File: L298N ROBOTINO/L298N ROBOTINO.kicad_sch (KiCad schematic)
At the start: 22 parts, among them J1 Conn_01x03, J2 Conn_01x03, J3 Conn_01x03, J4 Conn_01x02, J5 Conn_01x02, U1 L7805, U2 L298N

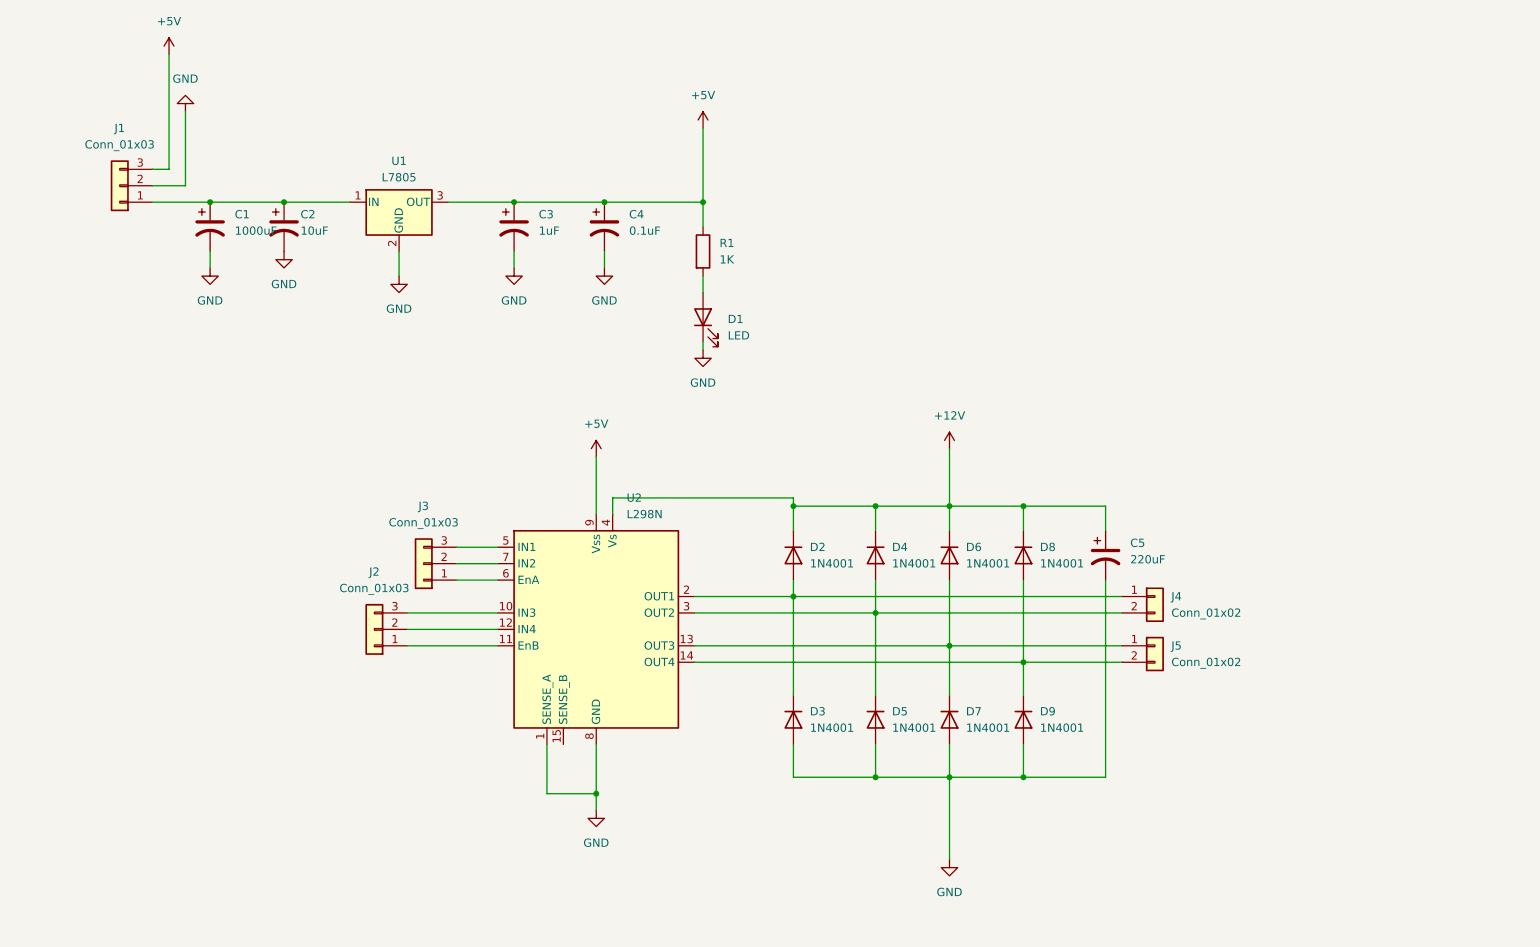
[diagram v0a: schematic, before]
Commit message: Nguon L298N date : 14/4/2026
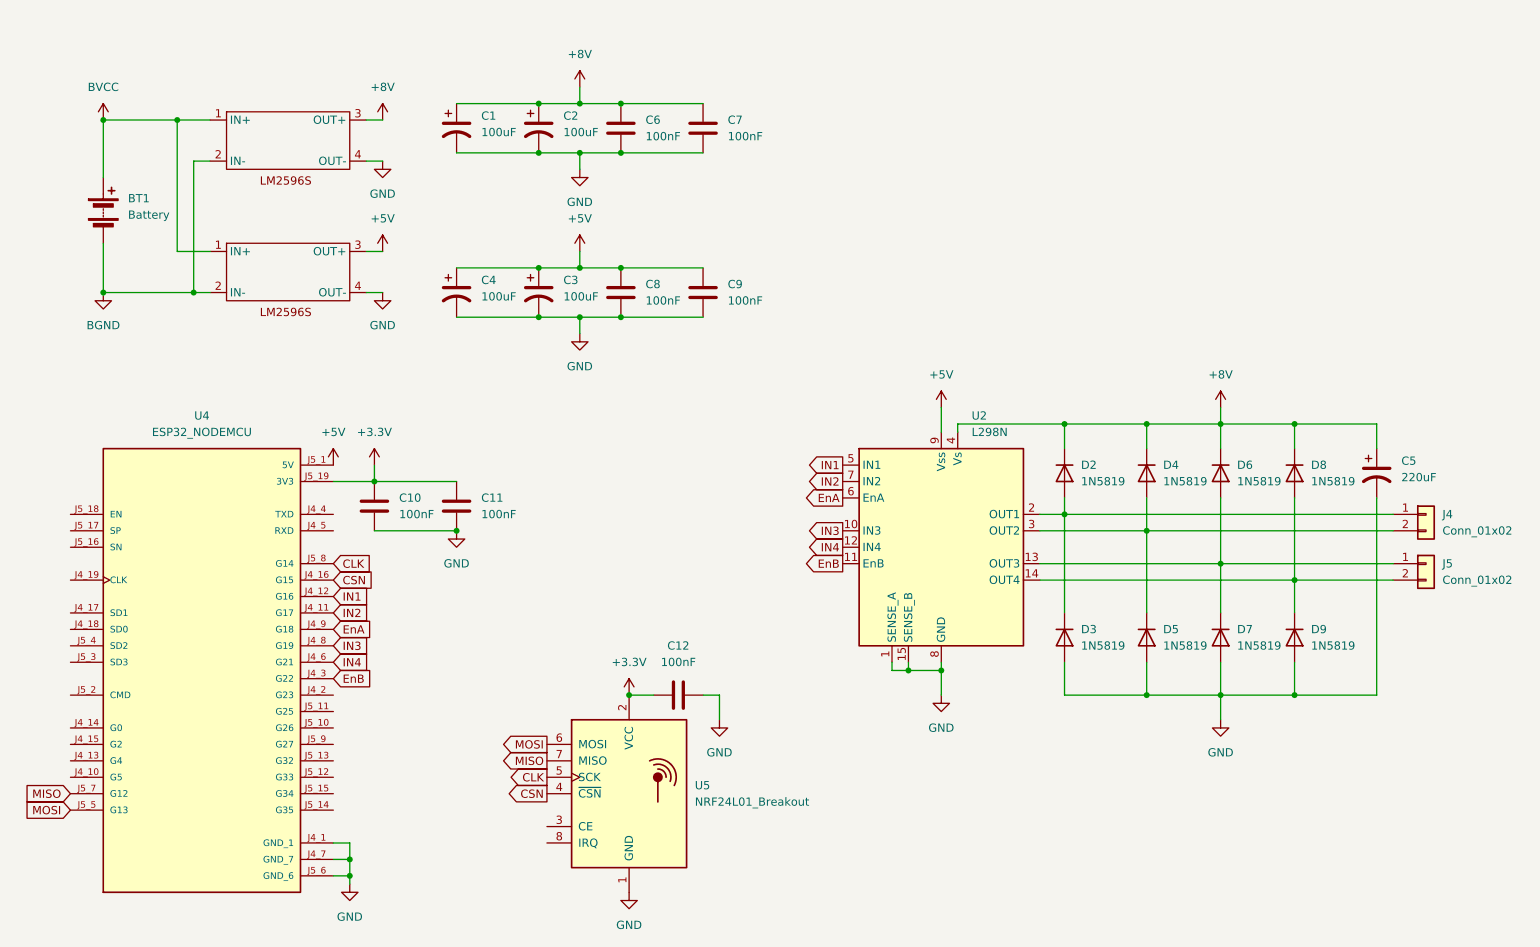
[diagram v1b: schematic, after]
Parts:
- removed D1: LED, symbol Device:LED
- removed J1, J2, J3: Conn_01x03, symbol Connector_Generic:Conn_01x03
- removed R1: 1K, symbol Device:R
- removed U1: L7805, symbol Regulator_Linear:L7805
- added BT1: Battery, symbol Device:Battery
- added C10, C11, C12, C6, C7, C8, C9: 100nF, Capacitor_THT:C_Disc_D3.0mm_W1.6mm_P2.50mm, symbol Device:C
- added U1, U3: (no value), ROBOTINO:LM2596S_Module, symbol ROBOTINO_Custom:LM2596S_Module
- added U4: ESP32_NODEMCU, ESP32_NODEMCU:MODULE_ESP32_NODEMCU, symbol ESP32_NODEMCU:ESP32_NODEMCU
- added U5: NRF24L01_Breakout, RF_Module:nRF24L01_Breakout, symbol RF:NRF24L01_Breakout
- C1: value 1000uF -> 100uF; footprint (none) -> Capacitor_THT:C_Radial_D6.3mm_H11.0mm_P2.50mm
- C2: value 10uF -> 100uF; footprint (none) -> Capacitor_THT:C_Radial_D6.3mm_H11.0mm_P2.50mm
- C3: value 1uF -> 100uF; footprint (none) -> Capacitor_THT:C_Radial_D6.3mm_H11.0mm_P2.50mm
- C4: value 0.1uF -> 100uF; footprint (none) -> Capacitor_THT:C_Radial_D6.3mm_H11.0mm_P2.50mm
- D2, D3, D4, D5, D6, D7, D8, D9: value 1N4001 -> 1N5819
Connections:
- net +12V is gone; now on net +8V: C5.1, D2.1 (K), D4.1 (K), D6.1 (K), D8.1 (K), U2.4 (Vs)
- net +5V: now also C8.1, C9.1, U3.3 (OUT+), U4.J5_1 (5V)
- net GND: now also U2.15 (SENSE_B), C10.2, C11.2, C12.2, C6.2, C7.2, C8.2, C9.2, U1.4 (OUT-), U3.4 (OUT-), U4.J4_1 (GND_1), U4.J4_7 (GND_7), U4.J5_6 (GND_6), U5.1 (GND)
- net IN3: now reaches U2.10 (IN3)
- net IN3: now also U4.J4_8 (G19)
- net EnB: now reaches U2.11 (EnB)
- net EnB: now also U4.J4_3 (G22)
- net IN4: now reaches U2.12 (IN4)
- net IN4: now also U4.J4_6 (G21)
- net IN1: now reaches U2.5 (IN1)
- net IN1: now also U4.J4_12 (G16)
- net EnA: now reaches U2.6 (EnA)
- net EnA: now also U4.J4_9 (G18)
- net IN2: now reaches U2.7 (IN2)
- net IN2: now also U4.J4_11 (G17)
- net +8V: now reaches C1.1, C2.1
- net +8V: now also C6.1, C7.1, U1.3 (OUT+)
- new net +3.3V: C10.1, C11.1, C12.1, U4.J5_19 (3V3), U5.2 (VCC)
- new net BGND: BT1.2 (-), U1.2 (IN-), U3.2 (IN-)
- new net BVCC: BT1.1 (+), U1.1 (IN+), U3.1 (IN+)
- new net CLK: U4.J5_8 (G14), U5.5 (SCK)
- new net CSN: U4.J4_16 (G15), U5.4 (~{CSN})
- new net MISO: U4.J5_7 (G12), U5.7 (MISO)
- new net MOSI: U4.J5_5 (G13), U5.6 (MOSI)
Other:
- moved on the sheet: C5, D2, D3, D4, D5, D6, D7, D8, D9, J4, J5, U2
